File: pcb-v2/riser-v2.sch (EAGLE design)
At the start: 36 parts, among them IC1 SI53152-A01AGM, IC2 TPS51386RJNR, J1 MDT350M01001VTEXT, J2 MDT350M01001VTEXT, J3 PCI-E-X4, J4 0022053031, T1 2N7002, Y1 ECS-327KE-TR

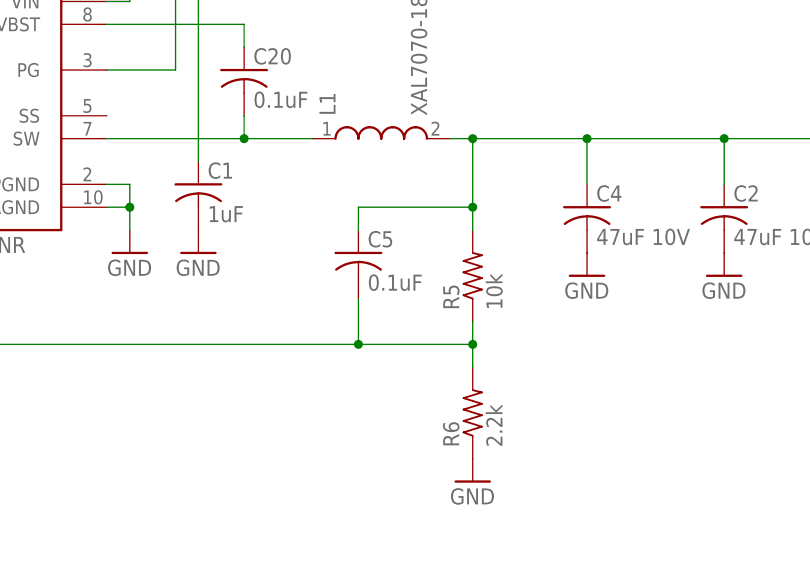
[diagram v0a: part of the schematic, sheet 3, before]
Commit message: Mark DNP in EAGLE files too
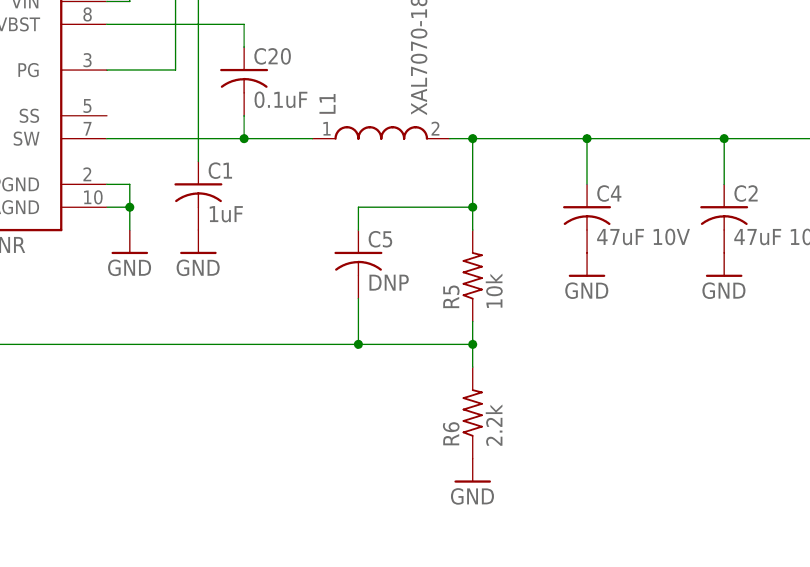
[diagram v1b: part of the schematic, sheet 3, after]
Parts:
- C5: value 0.1uF -> DNP
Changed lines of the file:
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@@
 <part name="C11" library="rcl" deviceset="C-US" device="C0603" value="10uF 10V"/>
 <part name="C10" library="rcl" deviceset="C-US" device="C0603" value="10uF 10V"/>
-<part name="C5" library="rcl" deviceset="C-US" device="C0402" value="0.1uF"/>
+<part name="C5" library="rcl" deviceset="C-US" device="C0402" value="DNP"/>
 <part name="P+5" library="supply1" deviceset="+12V" device=""/>
 <part name="P+6" library="supply1" deviceset="VCC" device=""/>
